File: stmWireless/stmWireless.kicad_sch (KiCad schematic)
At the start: 27 parts, among them J1 SWD, J2 CORTEX_DEBUG, J3 Conn_02x08_Top_Bottom, U1 STM32WLE5CBU6, U2 AP63203WU, Y1 Crystal_32MHz, Y2 Crystal_32.768kHz

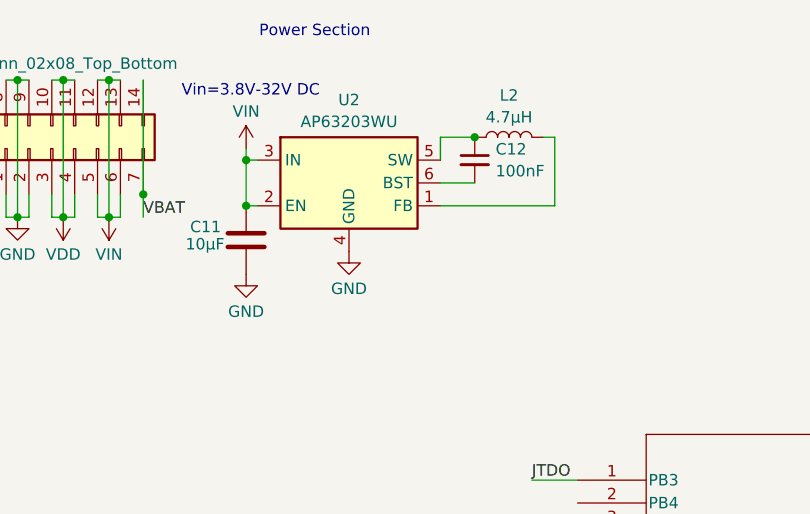
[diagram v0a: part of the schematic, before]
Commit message: add power supply components to PCB
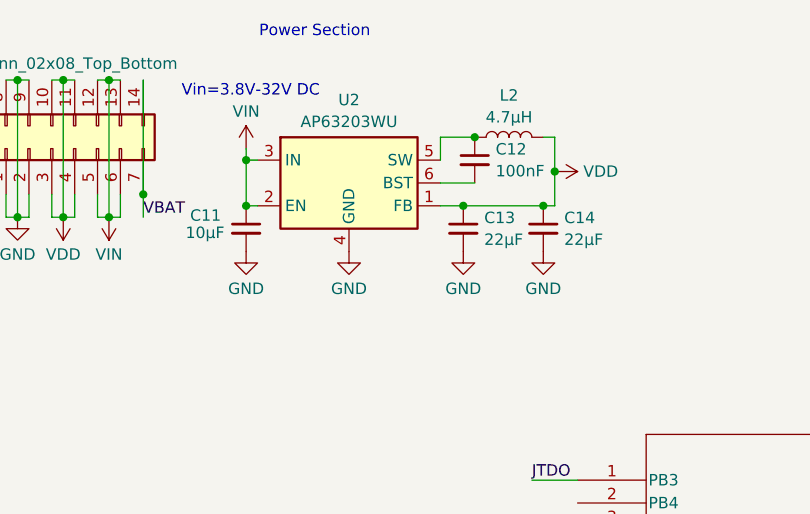
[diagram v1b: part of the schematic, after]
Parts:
- added C13, C14: 22µF, Capacitor_SMD:C_0603_1608Metric, symbol Device:C_Small
- C11: footprint (none) -> Capacitor_SMD:C_0603_1608Metric; symbol Device:C -> Device:C_Small
- C12: footprint (none) -> Capacitor_SMD:C_0603_1608Metric
- J3: footprint (none) -> Connector_PinHeader_2.54mm:PinHeader_2x07_P2.54mm_Vertical
- L2: footprint (none) -> Inductor_SMD:L_0603_1608Metric
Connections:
- net GND: now also C13.2, C14.2
- net VDD: now also L2.2, U2.1 (FB), C13.1, C14.1
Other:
- moved on the sheet: C11

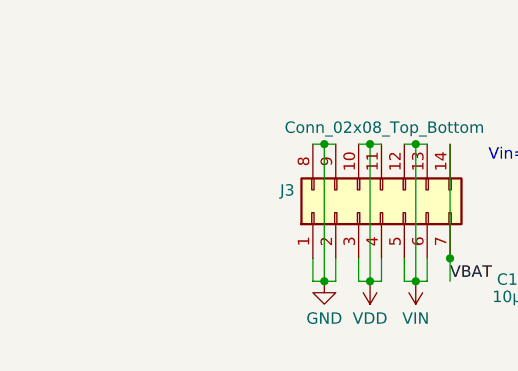
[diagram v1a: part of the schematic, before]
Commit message: added power LED
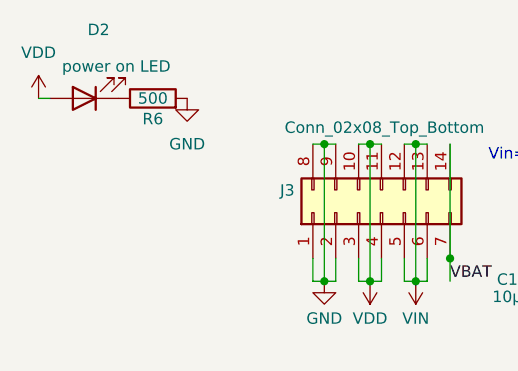
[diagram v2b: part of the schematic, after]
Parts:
- added D2: power on LED, LED_SMD:LED_0603_1608Metric, symbol Device:LED
- added R6: 500, Resistor_SMD:R_0603_1608Metric, symbol Device:R
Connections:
- net GND: now also R6.2
- net VDD: now also D2.2 (A)
- new net: D2.1 (K), R6.1

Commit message: begining of wireless thing
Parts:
- added C15: 68pF, symbol Device:C_Small
- added C16: 47nF, symbol Device:C_Small
- added C17: 100pF, symbol Device:C_Small
- added L3: L, symbol Device:L
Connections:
- net GND: now also C15.2, C16.2
- net at U1.23 (RFO_HP): now also C17.2, L3.1
- net at U1.24 (VR_PA): now also C15.1, C16.1, L3.2

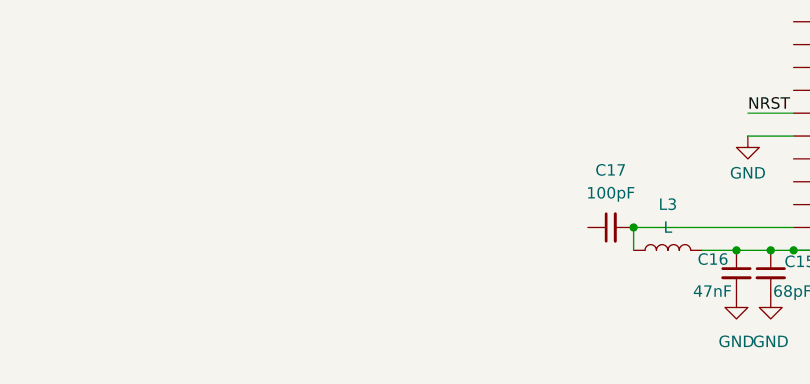
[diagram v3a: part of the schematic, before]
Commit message: add schematic item for BALF IPD
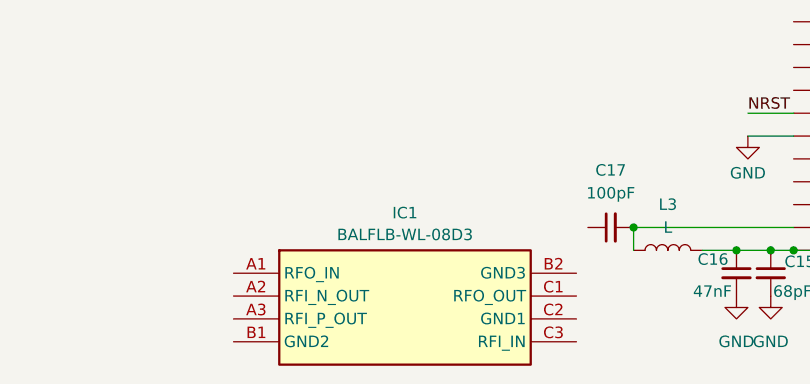
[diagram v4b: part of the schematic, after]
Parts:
- added IC1: BALFLB-WL-08D3, BALFLBWL08D3, symbol Project_library:BALFLB-WL-08D3
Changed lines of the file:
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@@
+	)
+	(symbol
+		(lib_id "Project_library:BALFLB-WL-08D3")
+		(at 46.99 132.08 0)
+		(unit 1)
+		(exclude_from_sim no)
+		(in_bom yes)
+		(on_board yes)
+		(dnp no)
+		(fields_autoplaced yes)
+		(property "Reference" "IC1"
+			(at 66.04 125.3955 0)
+			(effects
+				(font
+					(size 1.27 1.27)
+				)
+			)
+		)
+		(property "Value" "BALFLB-WL-08D3"
+			(at 66.04 127.8198 0)
+			(effects
+				(font
+					(size 1.27 1.27)
+				)
+			)
+		)
+		(property "Footprint" "BALFLBWL08D3"
+			(at 81.28 227 0)
+			(effects
+				(font
+					(size 1.27 1.27)
+				)
+				(justify left top)
+				(hide yes)
+			)
+		)
+		(property "Datasheet" "https://www.st.com/resource/en/datasheet/balflb-wl-08d3.pdf"
+			(at 81.28 327 0)
+			(effects
+				(font
+					(size 1.27 1.27)
+				)
+				(justify left top)
+				(hide yes)
+			)
+		)
+		(property "Description" "balun,filtering and matching of STM32WL 17dbm 490Mhz , QFN package 4 layers pcb"
+			(at 46.99 132.08 0)
+			(effects
+				(font
+					(size 1.27 1.27)
+				)
+				(hide yes)
+			)
+		)
+		(property "Height" "0.68"
+			(at 81.28 527 0)
+			(effects
+				(font
+					(size 1.27 1.27)
+				)
+				(justify left top)
+				(hide yes)
+			)
+		)
+		(property "Manufacturer_Name" "STMicroelectronics"
+			(at 81.28 627 0)
+			(effects
+				(font
+					(size 1.27 1.27)
+				)
+				(justify left top)
+				(hide yes)
+			)
+		)
+		(property "Manufacturer_Part_Number" "BALFLB-WL-08D3"
+			(at 81.28 727 0)
+			(effects
+				(font
+					(size 1.27 1.27)
+				)
+				(justify left top)
+				(hide yes)
+			)
+		)
+		(property "Mouser Part Number" ""
+			(at 81.28 827 0)
+			(effects
+				(font
+					(size 1.27 1.27)
+				)
+				(justify left top)
+				(hide yes)
+			)
+		)
+		(property "Mouser Price/Stock" ""
+			(at 81.28 927 0)
+			(effects
+				(font
+					(size 1.27 1.27)
+				)
+				(justify left top)
+				(hide yes)
+			)
+		)
+		(property "Arrow Part Number" ""
+			(at 81.28 1027 0)
+			(effects
+				(font
+					(size 1.27 1.27)
+				)
+				(justify left top)
+				(hide yes)
+			)
+		)
+		(property "Arrow Price/Stock" ""
+			(at 81.28 1127 0)
+			(effects
+				(font
+					(size 1.27 1.27)
+				)
+				(justify left top)
+				(hide yes)
+			)
+		)
+		(pin "C1"
+		)
+		(pin "B1"
+		)
+		(pin "A3"
+		)
+		(pin "A2"
+		)
+		(pin "A1"
+		)
+		(pin "C2"
+		)
+		(pin "B2"
+		)
+		(pin "C3"
+		)
+		(instances
+			(project ""
+				(path "/1b6f2151-7631-405e-8c4b-cce50e35ccd7"
+					(reference "IC1")
+					(unit 1)
+				)
+			)
+		)
 	)
 	(symbol

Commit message: more wiorless
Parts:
- added C18: 68nF, symbol Device:C_Small
- added C19: ~, symbol Device:C_Small
- added U3: BGS12WN6E6327, Package_LGA:Infineon_PG-TSNP-6-10_0.7x1.1mm_0.7x1.1mm_P0.4mm, symbol RF_Switch:BGS12WN6E6327
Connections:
- net GND: now also IC1.B1 (GND2), IC1.B2 (GND3), IC1.C2 (GND1), C19.1
- net at IC1.A1 (RFO_IN): now also C17.1
- net at IC1.A2 (RFI_N_OUT): now also U1.21 (RFI_N)
- net at IC1.A3 (RFI_P_OUT): now also U1.20 (RFI_P)
- net at IC1.C1 (RFO_OUT): now also C18.1
- net at IC1.C3 (RFI_IN): now also C19.2, U3.3 (RF1)
- new net: C18.2, U3.1 (RF2)
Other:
- moved on the sheet: IC1

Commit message: coped RF cercit from refres scamatic 1848
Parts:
- added C20, C27: 1nF, symbol Device:C_Small
- added C21: 100nf, symbol Device:C_Small
- added C22: 68pF, symbol Device:C_Small
- added C23, C24, C25: ~, symbol Device:C_Small
- added C26: 100nF, symbol Device:C_Small
- added J4: SMA, symbol Connector:Conn_Coaxial
- added L4: L, symbol Device:L
- added R7, R8: 100R, symbol Device:R
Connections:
- net GND: now also U3.2 (GND), C20.1, C21.1, C23.2, C24.1, C25.1, C26.1, C27.1, J4.1 (In)
- net VDD: now also R7.2
- net at U3.4 (VDD): now also C20.2, C21.2, R7.1
- net at U3.5 (RFIN): now also C22.2, C23.1
- net at U3.6 (CTRL): now also C26.2, C27.2, R8.1
- net at D1.2 (A): no longer U1.38 (PC13)
- new net: C22.1, C24.2, L4.2
- new net: C25.2, J4.2 (Ext), L4.1
- new net RF-CTRL: R8.2, U1.38 (PC13)
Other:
- moved on the sheet: D1, R5, U3

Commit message: assign footprints and minor cleanup
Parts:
- C15, C16, C17, C18, C19, C20, C21, C22, C23, C24, C25, C26, C27: footprint (none) -> Capacitor_SMD:C_0603_1608Metric
- IC1: footprint BALFLBWL08D3 -> Project_library:BALFLBWL08D3
- R7, R8: footprint (none) -> Resistor_SMD:R_0603_1608Metric
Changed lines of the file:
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@@
 	)
 	(junction
-		(at 109.22 129.54)
-		(diameter 0)
-		(color 0 0 0 0)
-	)
-	(junction
 		(at 241.3 68.58)
 		(diameter 0)
@@
 	(wire
 		(pts
-			(xy 113.03 129.54) (xy 109.22 129.54)
-		)
-		(stroke
-			(width 0)
-			(type default)
-		)
-	)
-	(wire
-		(pts
 			(xy 160.02 147.32) (xy 163.83 147.32)
 		)
@@
 			)
 		)
-		(property "Footprint" "BALFLBWL08D3"
+		(property "Footprint" "Project_library:BALFLBWL08D3"
 			(at 120.65 247.32 0)
 			(effects
@@
 			)
 		)
-		(property "Footprint" ""
+		(property "Footprint" "Capacitor_SMD:C_0603_1608Metric"
 			(at 177.8 154.94 0)
 			(effects
@@
 			)
 		)
-		(property "Footprint" ""
+		(property "Footprint" "Capacitor_SMD:C_0603_1608Metric"
 			(at 124.46 162.56 0)
 			(effects
@@
 			)
 		)
-		(property "Footprint" ""
+		(property "Footprint" "Capacitor_SMD:C_0603_1608Metric"
 			(at 153.67 144.78 0)
 			(effects
@@
 			)
 		)
-		(property "Footprint" ""
+		(property "Footprint" "Resistor_SMD:R_0603_1608Metric"
 			(at 167.64 149.098 90)
 			(effects
@@
 			)
 		)
-		(property "Footprint" ""
+		(property "Footprint" "Capacitor_SMD:C_0603_1608Metric"
 			(at 185.42 154.94 0)
 			(effects
@@
 			)
 		)
-		(property "Footprint" ""
+		(property "Footprint" "Capacitor_SMD:C_0603_1608Metric"
 			(at 88.9 127 0)
 			(effects
@@
 			)
 		)
-		(property "Footprint" ""
+		(property "Footprint" "Capacitor_SMD:C_0603_1608Metric"
 			(at 135.89 154.94 0)
 			(effects
@@
 			)
 		)
-		(property "Footprint" ""
+		(property "Footprint" "Capacitor_SMD:C_0603_1608Metric"
 			(at 160.02 184.15 0)
 			(effects
@@
 			)
 		)
-		(property "Footprint" ""
+		(property "Footprint" "Capacitor_SMD:C_0603_1608Metric"
 			(at 106.68 132.08 0)
 			(effects
@@
 			)
 		)
-		(property "Footprint" ""
+		(property "Footprint" "Capacitor_SMD:C_0603_1608Metric"
 			(at 102.87 132.08 0)
 			(effects
@@
 			)
 		)
-		(property "Footprint" ""
+		(property "Footprint" "Capacitor_SMD:C_0603_1608Metric"
 			(at 171.45 184.15 0)
 			(effects
@@
 			)
 		)
-		(property "Footprint" ""
+		(property "Footprint" "Capacitor_SMD:C_0603_1608Metric"
 			(at 133.35 187.96 0)
 			(effects
@@
 			)
 		)
-		(property "Footprint" ""
+		(property "Footprint" "Capacitor_SMD:C_0603_1608Metric"
 			(at 146.05 187.96 0)
 			(effects
@@
 			)
 		)
-		(property "Footprint" ""
+		(property "Footprint" "Capacitor_SMD:C_0603_1608Metric"
 			(at 160.02 144.78 0)
 			(effects
@@
 			)
 		)
-		(property "Footprint" ""
+		(property "Footprint" "Resistor_SMD:R_0603_1608Metric"
 			(at 194.31 154.178 90)
 			(effects

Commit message: move components badly into place
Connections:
- net GND: now also C23.1; no longer C23.2
- net at C22.2, U3.5 (RFIN): now also C23.2; no longer C23.1
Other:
- moved on the sheet: C23
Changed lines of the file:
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@@
 	)
 	(junction
-		(at 168.91 184.15)
-		(diameter 0)
-		(color 0 0 0 0)
-	)
-	(junction
 		(at 46.99 41.91)
 		(diameter 0)
@@
 	)
 	(junction
+		(at 168.91 184.15)
+		(diameter 0)
+		(color 0 0 0 0)
+	)
+	(junction
 		(at 133.35 184.15)
 		(diameter 0)
@@
 	(symbol
 		(lib_id "power:GND")
-		(at 173.99 184.15 0)
+		(at 168.91 189.23 0)
 		(unit 1)
 		(exclude_from_sim no)
@@
 		(fields_autoplaced yes)
 		(property "Reference" "#PWR042"
-			(at 173.99 190.5 0)
+			(at 168.91 195.58 0)
 			(effects
 				(font
@@
 		)
 		(property "Value" "GND"
-			(at 173.99 189.23 0)
+			(at 168.91 194.31 0)
 			(effects
 				(font
@@
 		)
 		(property "Footprint" ""
-			(at 173.99 184.15 0)
+			(at 168.91 189.23 0)
 			(effects
 				(font
@@
 		)
 		(property "Datasheet" ""
-			(at 173.99 184.15 0)
+			(at 168.91 189.23 0)
 			(effects
 				(font
@@
 		)
 		(property "Description" "Power symbol creates a global label with name \"GND\" , ground"
-			(at 173.99 184.15 0)
+			(at 168.91 189.23 0)
 			(effects
 				(font
@@
 	(symbol
 		(lib_id "Device:C_Small")
-		(at 171.45 184.15 90)
+		(at 168.91 186.69 180)
 		(unit 1)
 		(exclude_from_sim no)
@@
 		(dnp no)
 		(property "Reference" "C23"
-			(at 173.736 181.102 90)
+			(at 168.402 188.976 0)
 			(effects
 				(font
@@
 		)
 		(property "Value" "~"
-			(at 169.672 190.246 0)
+			(at 175.006 188.468 0)
 			(effects
 				(font
@@
 		)
 		(property "Footprint" "Capacitor_SMD:C_0603_1608Metric"
-			(at 171.45 184.15 0)
+			(at 168.91 186.69 0)
 			(effects
 				(font
@@
 		)
 		(property "Datasheet" "~"
-			(at 171.45 184.15 0)
+			(at 168.91 186.69 0)
 			(effects
 				(font
@@
 		)
 		(property "Description" "Unpolarized capacitor, small symbol"
-			(at 171.45 184.15 0)
+			(at 168.91 186.69 0)
 			(effects
 				(font
